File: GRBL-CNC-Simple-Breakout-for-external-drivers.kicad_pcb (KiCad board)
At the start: 2 copper layers, 57.2 x 53.3 mm, 15 parts, among them P1 Power, P2 Analog, P3 Digital, P4 Digital, P5 CONN_01X01, P6 CONN_01X01, P7 CONN_01X01, P8 CONN_01X01

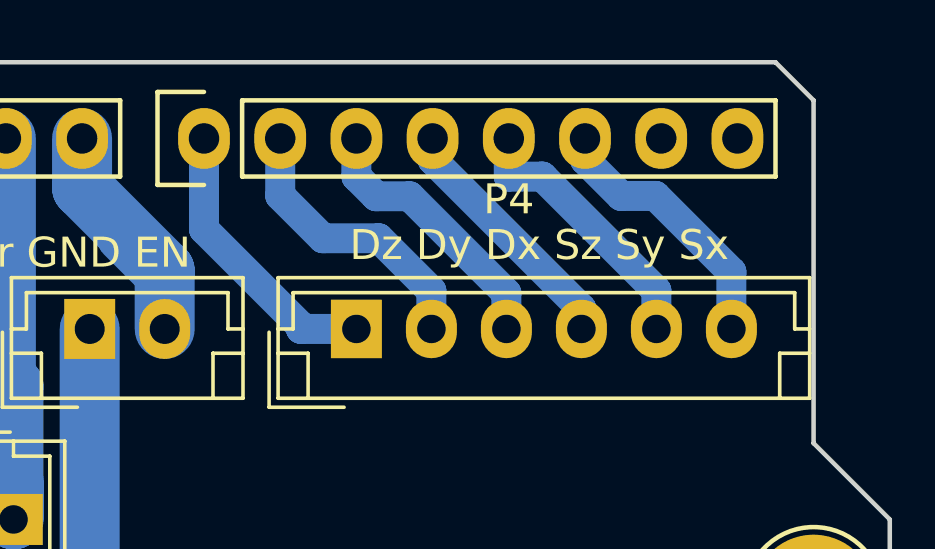
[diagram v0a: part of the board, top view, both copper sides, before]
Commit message: increased traces width, to produce it without any z homing capability (aka allow breadboard controller with minimal wireing to produce this)
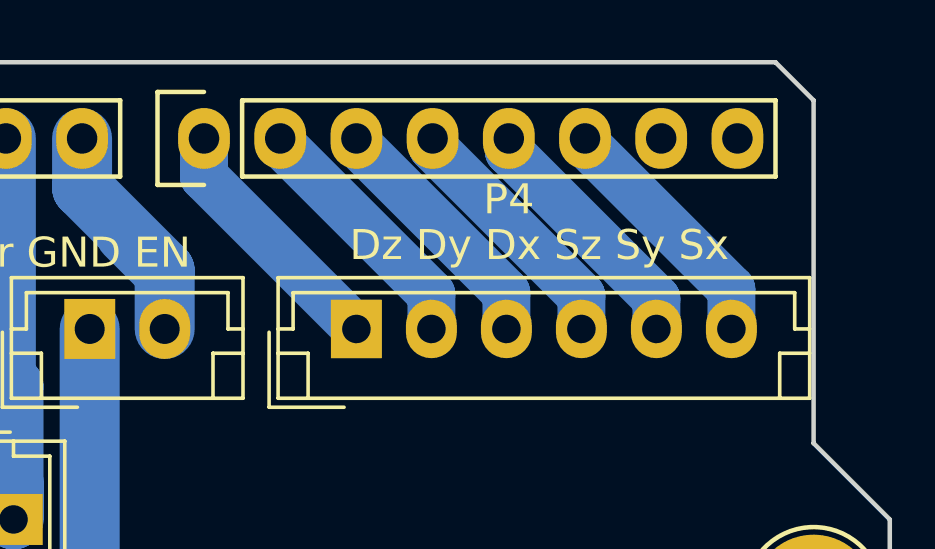
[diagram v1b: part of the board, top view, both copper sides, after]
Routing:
- net DirY: track 9.53 -> 8.44 mm
- net DirZ: track 9.54 -> 8.45 mm
- net StepX: track 9.04 -> 8.37 mm
- net DirX: track 9.08 -> 8.42 mm
- net StepY: track 9.04 -> 8.39 mm
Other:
- net class Default: clearance 0.4 -> 0.1; trace_width 2 -> 1.6
- rule trace_clearance: 0.4 -> 0.1
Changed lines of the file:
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@@
     (thickness 1.6)
     (drawings 28)
-    (tracks 99)
+    (tracks 90)
     (zones 0)
     (modules 15)
@@
   )
   (layers
-    (0 F.Cu signal hide)
+    (0 F.Cu signal)
     (31 B.Cu signal)
     (32 B.Adhes user)
@@
   )
   (setup
-    (last_trace_width 2)
-    (trace_clearance 0.4)
+    (last_trace_width 1.6)
+    (trace_clearance 0.1)
     (zone_clearance 0.1)
     (zone_45_only no)
@@
     (visible_elements 7FFFFFFF)
     (pcbplotparams
-      (layerselection 0x00030_80000001)
+      (layerselection 0x01030_ffffffff)
       (usegerberextensions false)
       (usegerberattributes false)
@@
       (outputformat 1)
       (mirror false)
-      (drillshape 1)
+      (drillshape 0)
       (scaleselection 1)
-      (outputdirectory ""))
+      (outputdirectory "cnc/"))
   )
   (net 0 "")
@@
   (net 36 "Net-(P1-Pad7)")
   (net_class Default "This is the default net class."
-    (clearance 0.4)
-    (trace_width 2)
+    (clearance 0.1)
+    (trace_width 1.6)
     (via_dia 0.6)
     (via_drill 0.4)
@@
   (segment (start 135.128 97.79) (end 135.128 106.348252) (width 2) (layer B.Cu) (net 15))
   (segment (start 147.193 90.13) (end 147.193 97.155) (width 2) (layer B.Cu) (net 15))
-  (segment (start 159.948 81.915) (end 161.798 81.915) (width 1) (layer B.Cu) (net 16))
-  (segment (start 156.718 75.565) (end 156.718 78.592981) (width 1) (layer B.Cu) (net 16))
-  (segment (start 159.948 81.822981) (end 156.718 78.592981) (width 1) (layer B.Cu) (net 16))
-  (segment (start 159.948 81.915) (end 159.948 81.822981) (width 1) (layer B.Cu) (net 16))
-  (segment (start 162.5454 78.8924) (end 164.298 80.645) (width 1) (layer B.Cu) (net 17))
-  (segment (start 160.6804 78.8924) (end 162.5454 78.8924) (width 1) (layer B.Cu) (net 17))
-  (segment (start 159.258 77.47) (end 160.6804 78.8924) (width 1) (layer B.Cu) (net 17))
-  (segment (start 164.298 80.645) (end 164.298 81.915) (width 1) (layer B.Cu) (net 17))
-  (segment (start 159.258 75.565) (end 159.258 77.47) (width 1) (layer B.Cu) (net 17))
-  (segment (start 166.798 80.7174) (end 166.798 81.915) (width 1) (layer B.Cu) (net 18))
-  (segment (start 163.57299 77.49239) (end 166.798 80.7174) (width 1) (layer B.Cu) (net 18))
-  (segment (start 162.45539 77.49239) (end 163.57299 77.49239) (width 1) (layer B.Cu) (net 18))
-  (segment (start 161.798 76.835) (end 162.45539 77.49239) (width 1) (layer B.Cu) (net 18))
-  (segment (start 161.798 75.565) (end 161.798 76.835) (width 1) (layer B.Cu) (net 18))
-  (segment (start 169.298 81.237487) (end 169.298 81.915) (width 1) (layer B.Cu) (net 19))
-  (segment (start 164.338 76.277487) (end 169.298 81.237487) (width 1) (layer B.Cu) (net 19))
-  (segment (start 164.338 75.565) (end 164.338 76.277487) (width 1) (layer B.Cu) (net 19))
-  (segment (start 171.798 80.6374) (end 171.798 81.915) (width 1) (layer B.Cu) (net 20))
-  (segment (start 167.9956 76.835) (end 171.798 80.6374) (width 1) (layer B.Cu) (net 20))
-  (segment (start 166.878 76.835) (end 167.9956 76.835) (width 1) (layer B.Cu) (net 20))
-  (segment (start 166.878 75.565) (end 166.878 76.835) (width 1) (layer B.Cu) (net 20))
-  (segment (start 169.418 75.565) (end 169.418 76.277488) (width 1) (layer B.Cu) (net 21))
-  (segment (start 169.418 76.277488) (end 170.621522 77.48101) (width 1) (layer B.Cu) (net 21))
-  (segment (start 171.76901 77.48101) (end 174.298 80.01) (width 1) (layer B.Cu) (net 21))
-  (segment (start 170.621522 77.48101) (end 171.76901 77.48101) (width 1) (layer B.Cu) (net 21))
-  (segment (start 174.298 80.01) (end 174.298 81.915) (width 1) (layer B.Cu) (net 21))
+  (segment (start 156.718 76.835) (end 161.798 81.915) (width 1.6) (layer B.Cu) (net 16))
+  (segment (start 156.718 75.565) (end 156.718 76.835) (width 1.6) (layer B.Cu) (net 16))
+  (segment (start 159.258 75.7174) (end 164.298 80.7574) (width 1.6) (layer B.Cu) (net 17))
+  (segment (start 164.298 80.7574) (end 164.298 81.915) (width 1.6) (layer B.Cu) (net 17))
+  (segment (start 159.258 75.565) (end 159.258 75.7174) (width 1.6) (layer B.Cu) (net 17))
+  (segment (start 166.798 80.7174) (end 166.798 81.915) (width 1.6) (layer B.Cu) (net 18))
+  (segment (start 161.798 75.7174) (end 166.798 80.7174) (width 1.6) (layer B.Cu) (net 18))
+  (segment (start 161.798 75.565) (end 161.798 75.7174) (width 1.6) (layer B.Cu) (net 18))
+  (segment (start 169.298 80.813223) (end 169.298 81.915) (width 1.6) (layer B.Cu) (net 19))
+  (segment (start 164.338 75.853223) (end 169.298 80.813223) (width 1.6) (layer B.Cu) (net 19))
+  (segment (start 164.338 75.565) (end 164.338 75.853223) (width 1.6) (layer B.Cu) (net 19))
+  (segment (start 171.798 80.909047) (end 171.798 81.915) (width 1.6) (layer B.Cu) (net 20))
+  (segment (start 166.878 75.989047) (end 171.798 80.909047) (width 1.6) (layer B.Cu) (net 20))
+  (segment (start 166.878 75.565) (end 166.878 75.989047) (width 1.6) (layer B.Cu) (net 20))
+  (segment (start 169.418 75.7174) (end 169.418 75.565) (width 1.6) (layer B.Cu) (net 21))
+  (segment (start 174.298 80.5974) (end 169.418 75.7174) (width 1.6) (layer B.Cu) (net 21))
+  (segment (start 174.298 81.915) (end 174.298 80.5974) (width 1.6) (layer B.Cu) (net 21))
   (zone (net 7) (net_name GND-USB) (layer B.Cu) (hatch edge 0.508)
     (connect_pads (clearance 0.1))
